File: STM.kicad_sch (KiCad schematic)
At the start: 29 parts, among them J7 PIN HEADER 2.54MM PITCH STR D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, U1 STM32L433CCU6, X1 CRYSTAL 32.0000MHZ 10PF SMD

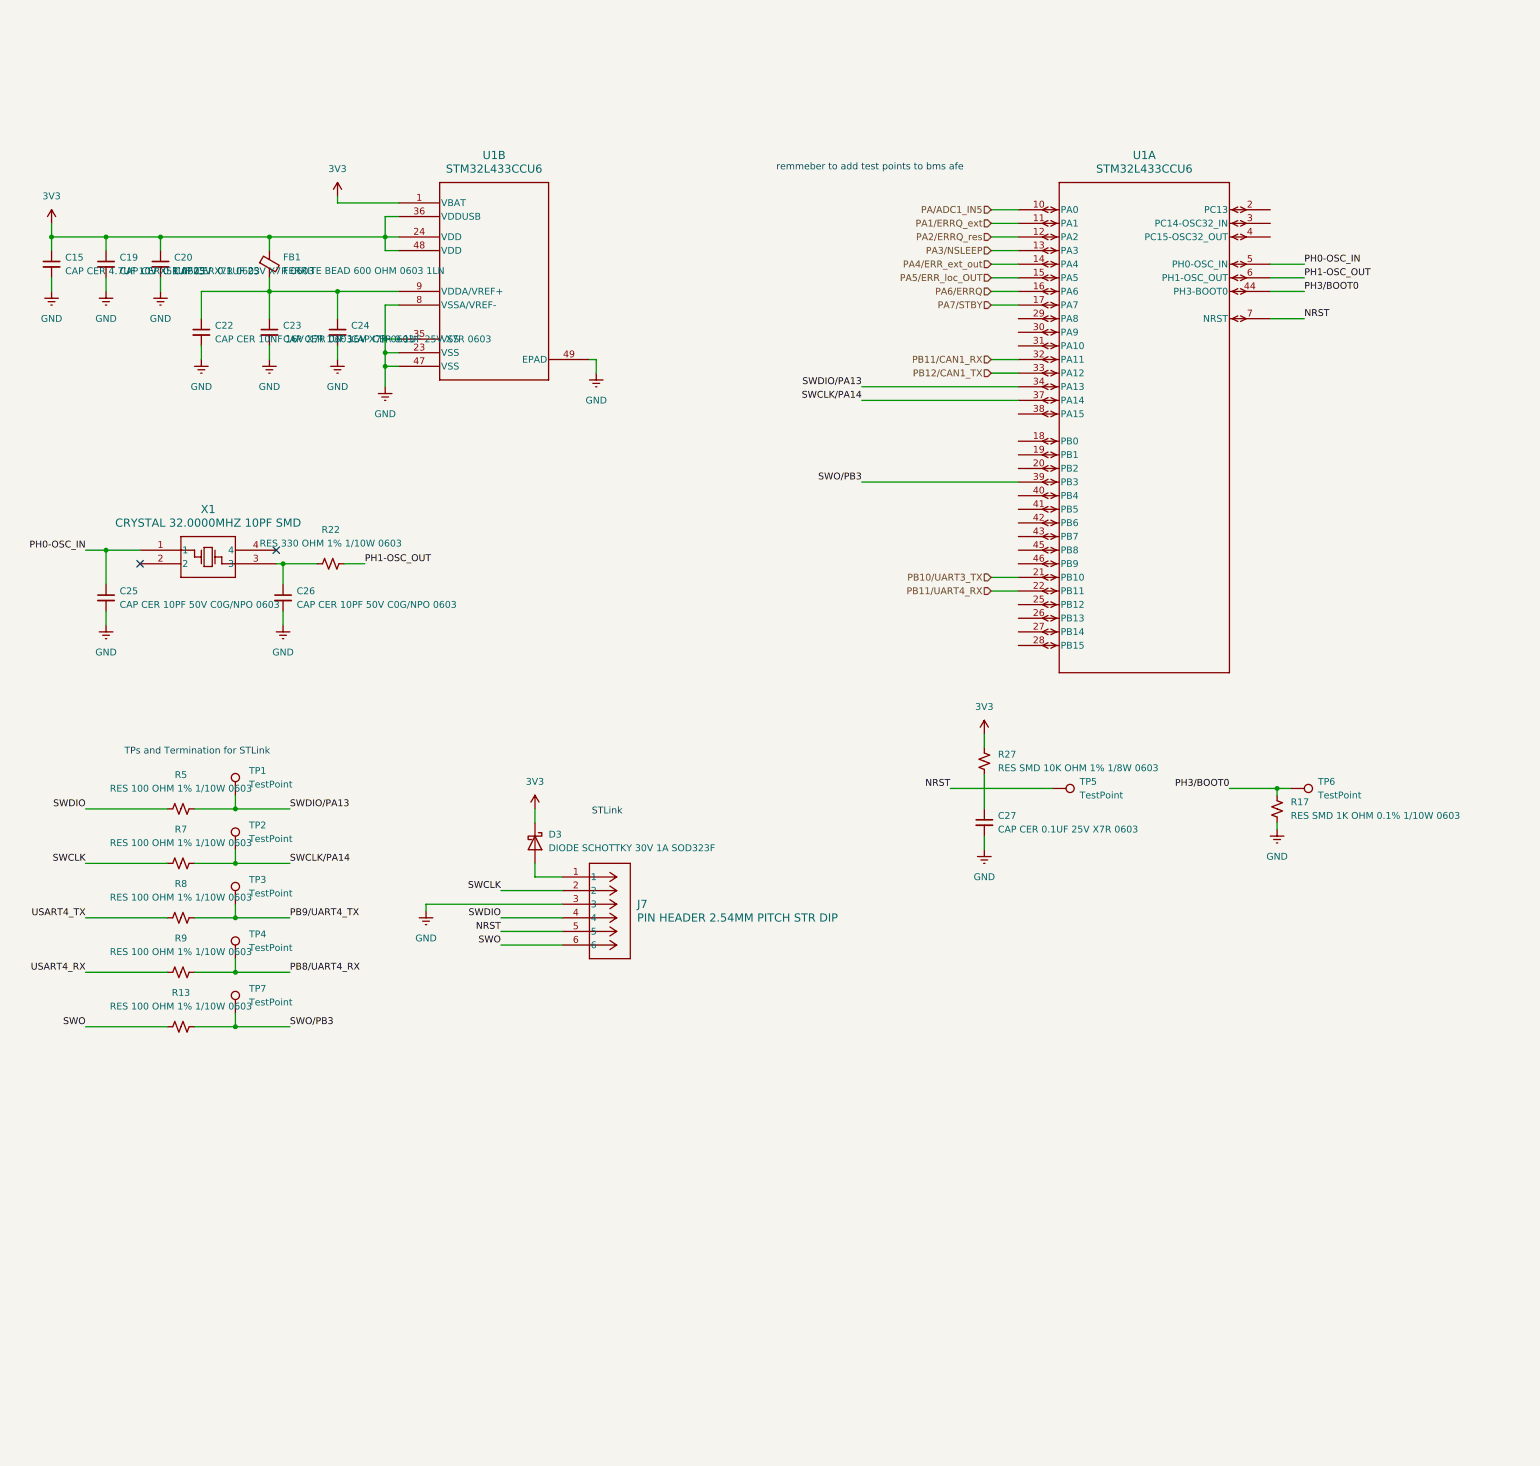
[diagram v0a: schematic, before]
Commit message: cleaned up schematic
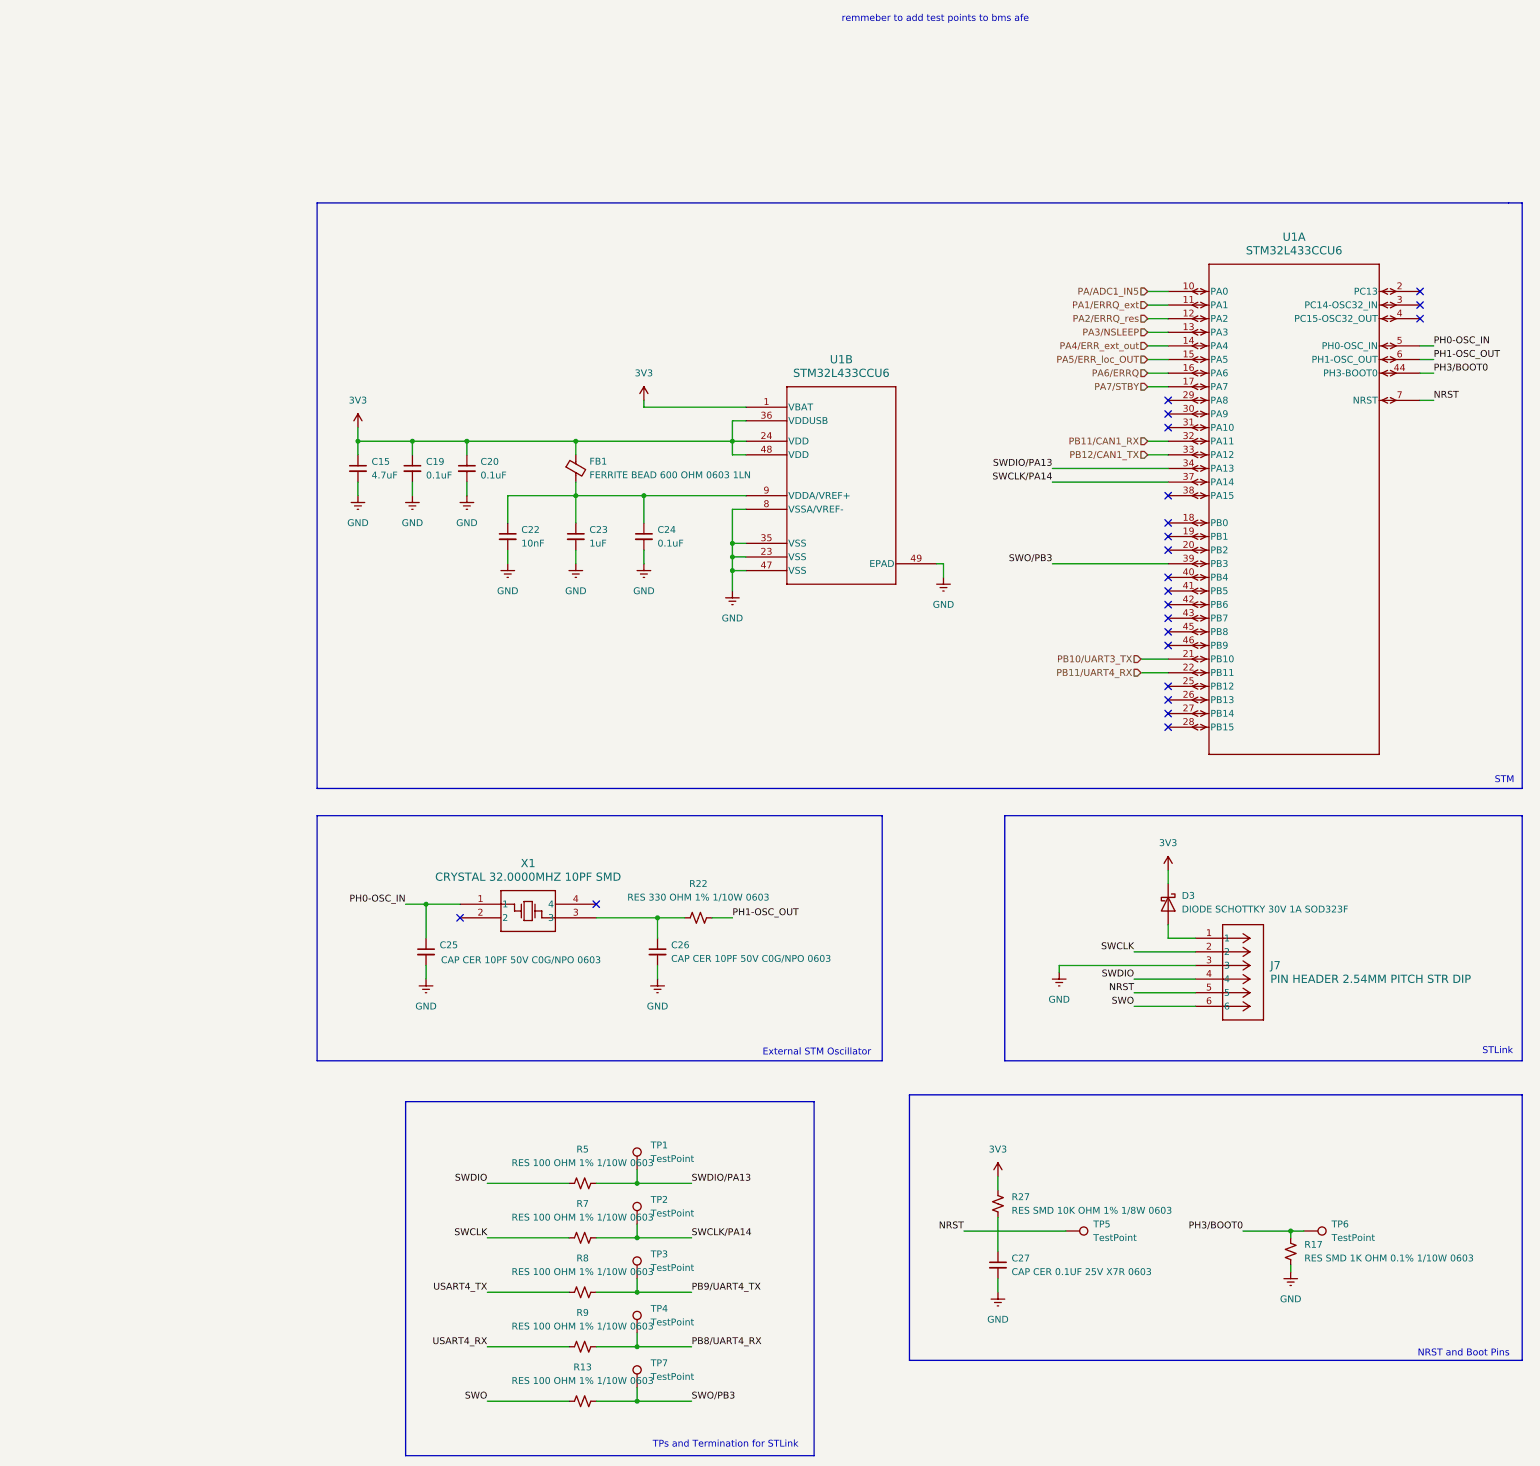
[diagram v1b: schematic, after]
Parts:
- C15: value CAP CER 4.7UF 10V X5R 0603 -> 4.7uF
- C19, C20, C24: value CAP CER 0.1UF 25V X7R 0603 -> 0.1uF
- C22: value CAP CER 10NF 16V X7R 0603 -> 10nF
- C23: value CAP CER 1UF 16V X7R 0603 -> 1uF
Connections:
- no-connect marks 2 -> 22
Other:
- note added: "External STM Oscillator"
- note added: "NRST and Boot Pins"
- note added: "STM"
- moved on the sheet: C15, C19, C20, C22, C23, C24, C25, C26, C27, D3, FB1, J7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

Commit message: minor changes
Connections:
- net PB11/CAN1_RX renamed PA11/CAN1_RX
- net PB12/CAN1_TX renamed PA12/CAN1_TX
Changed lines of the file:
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@@
 		)
 	)
-	(hierarchical_label "PB11{slash}CAN1_RX"
+	(hierarchical_label "PA11{slash}CAN1_RX"
 		(shape input)
 		(at 238.76 73.66 180)
@@
 		)
 	)
-	(hierarchical_label "PB12{slash}CAN1_TX"
+	(hierarchical_label "PA12{slash}CAN1_TX"
 		(shape input)
 		(at 238.76 76.2 180)

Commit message: minor changes
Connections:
- net PB8/UART4_RX is gone; now on net USART4_RX: R9.2, TP4.1
- net PB9/UART4_TX is gone; now on net USART4_TX: R8.2, TP3.1
- net PB10/UART3_TX: now also R8.1; no longer U1.21 (PB10)
- net PB11/UART4_RX: now also R9.1; no longer U1.22 (PB11)
- net USART4_RX: now also U1.22 (PB11); no longer R9.1
- net USART4_TX: now also U1.21 (PB10); no longer R8.1
- net PA/ADC1_IN5 renamed PA0/ADC1_IN5
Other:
- moved on the sheet: R13, TP7
